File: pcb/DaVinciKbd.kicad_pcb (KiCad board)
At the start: 2 copper layers, 215 x 125 mm, 79 parts, among them J1 Conn_01x04, J2 USB_C_Receptacle_USB2.0, U1 CherryMX_LED, U10 CherryMX_LED, U11 CherryMX_LED, U12 CherryMX_LED, U13 CherryMX_LED, U14 CherryMX15_LED, U15 CherryMX_LED, U16 CherryMX_LED, U17 CherryMX_LED, U18 CherryMX_LED, U19 CherryMX_LED, U2 CherryMX_LED, U20 CherryMX_LED, U21 CherryMX_LED, U22 CherryMX_LED, U23 CherryMX275_LED, U24 CherryMX_LED, U25 CherryMX_LED, U26 CherryMX_LED, U27 CherryMX_LED, U28 CherryMX_LED, U29 CherryMX_LED, U3 CherryMX15_LED, U30 CherryMX_LED, U31 CherryMX_LED, U32 CherryMX_LED, U33 CherryMX_LED, U34 CherryMX_LED, U35 CherryMX_LED, U36 CherryMX_LED, U37 CherryMX_LED, U38 CherryMX_LED, U39 CherryMX125_LED, U4 CherryMX_LED, U40 CherryMX15_LED, U41 CherryMX_LED, U42 CherryMX_LED, U43 BP, U44 CherryMX15_LED, U45 CherryMX_LED, U5 CherryMX_LED, U6 CherryMX_LED, U7 CherryMX_LED, U8 CherryMX_LED, U9 CherryMX_LED

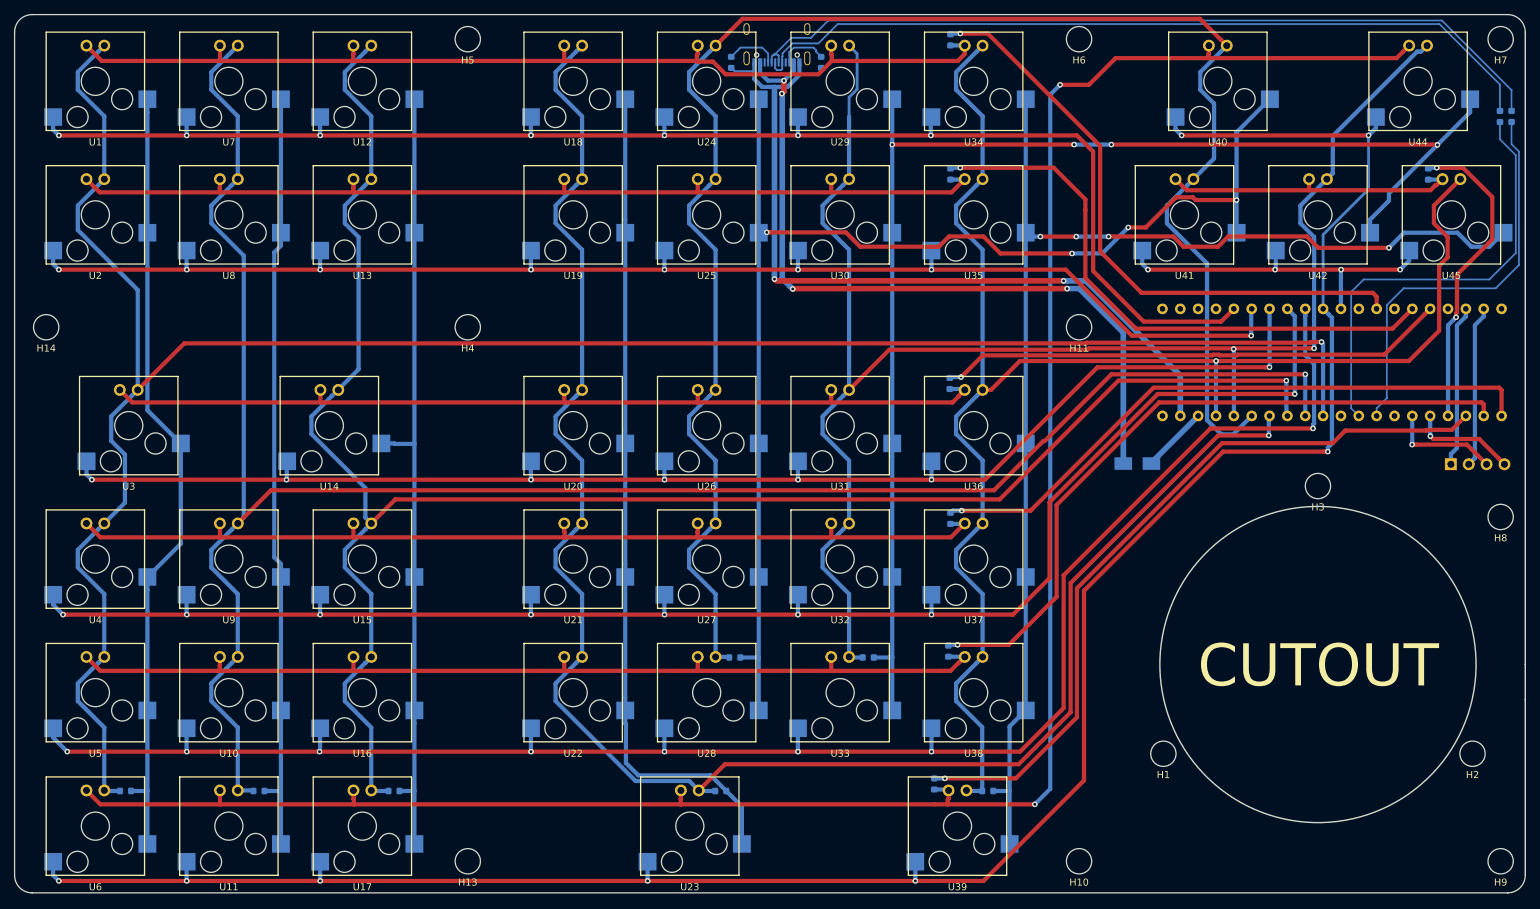
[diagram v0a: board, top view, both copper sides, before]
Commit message: Added polarities on PCB  and component values on both sch&PCB
Updated the values of all the components in schematics and PCB.
Modified silkscreen to print diode polarity, and resistor values
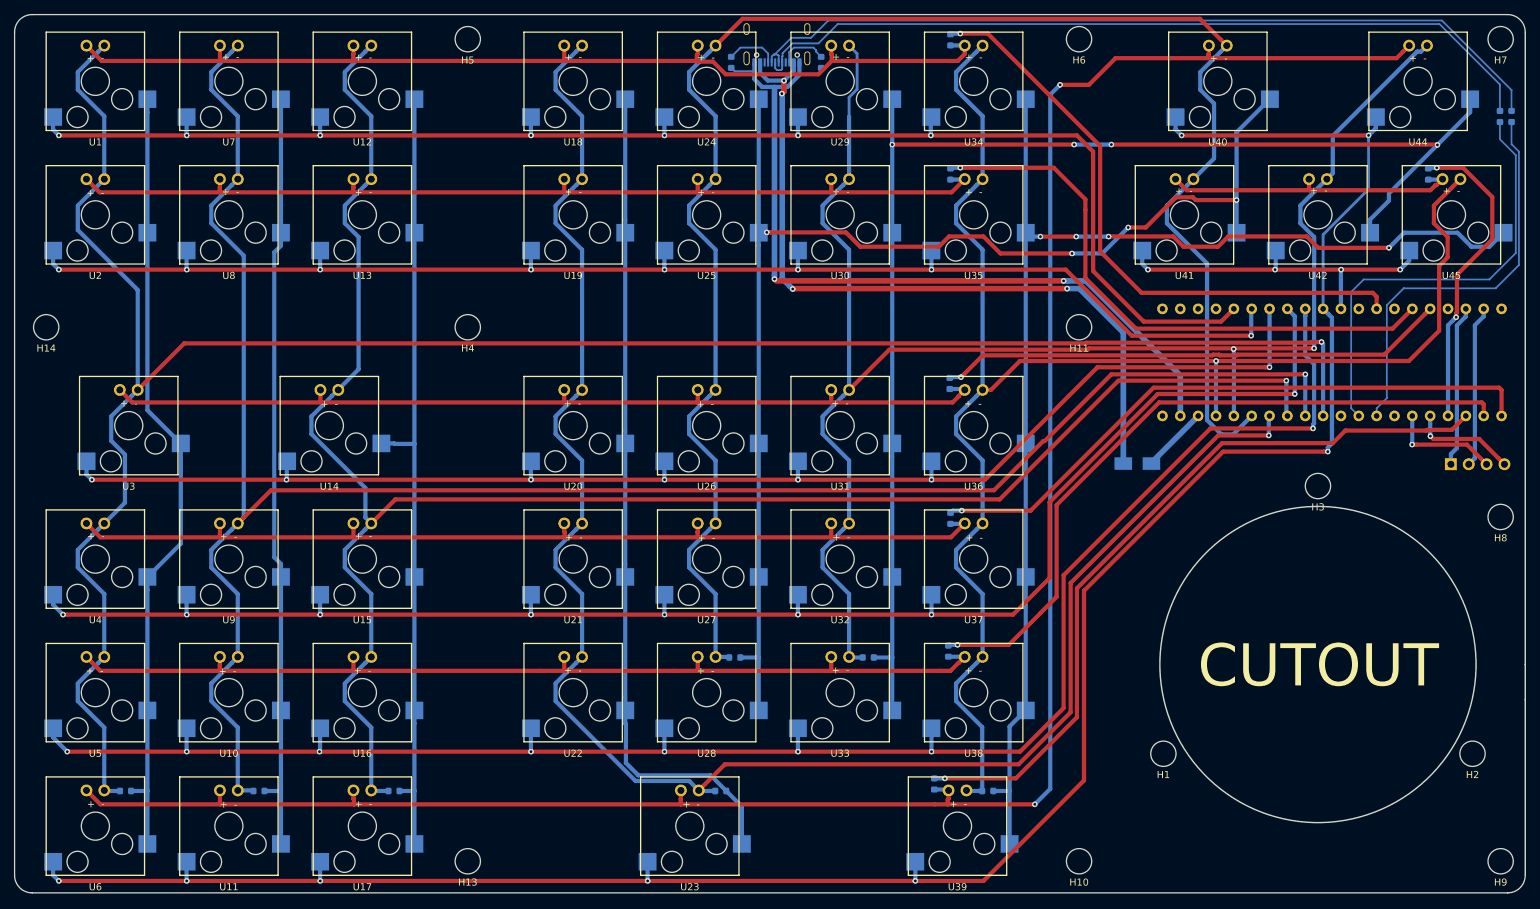
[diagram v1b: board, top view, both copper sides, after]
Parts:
- D1: value D_Schottky_Small -> 1N5819
- R1, R2, R3, R4, R5, R6, R7: value R_Small -> 330
- R10, R11: value R_Small -> 22
- R43, R46, R47, R48, R49, R50, R51: value R_Small -> 68
- R8, R9: value R_Small -> 1K
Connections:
- J2 pad A8: (no net) -> unconnected-(J2-PadA8)
- J2 pad B8: (no net) -> unconnected-(J2-PadB8)
- J2 pad S1: Net-(J2-PadS1) -> unconnected-(J2-PadS1)
- U43 pad NRST: (no net) -> unconnected-(U43-PadNRST)
- U43 pad PA10: (no net) -> unconnected-(U43-PadPA10)
- U43 pad PA15: (no net) -> unconnected-(U43-PadPA15)
- U43 pad PA7: (no net) -> unconnected-(U43-PadPA7)
- U43 pad PB1: (no net) -> unconnected-(U43-PadPB1)
- U43 pad PC13: (no net) -> unconnected-(U43-PadPC13)
- U43 pad PC14: (no net) -> unconnected-(U43-PadPC14)
- U43 pad PC15: (no net) -> unconnected-(U43-PadPC15)
- U43 pad VBAT: (no net) -> unconnected-(U43-PadVBAT)
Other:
- net class Default removed
- board text added: "+ -"
- board text added: "- +"
- board text added: "R1-7 330Ώ R8-9 1kΏ R10-11 22Ώ R43-51 68Ώ"
- board text added: "U1-45 CherryMX U1-45 3mm LED D1 1N5819 U43 Bluepill J1 PinHeader J2 USBC"
